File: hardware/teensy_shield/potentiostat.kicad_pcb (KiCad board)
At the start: 2 copper layers, 144.8 x 88.9 mm, 99 parts, among them K1 CONN_3, P1 CONN_2, P10 CONN_2, P11 CONN_2, P12 CONN_2, P13 CONN_5X2, P14 CONN_5X2, P15 CONN_2X2, P16 CONN_2X2, P17 CONN_2, P18 CONN_2, P19 CONN_2, P2 CONN_2, P20 CONN_2, P21 CONN_2, P3 CONN_2, P4 CONN_2, P5 CONN_2, P6 CONN_2, P7 CONN_2, P8 CONN_2, P9 CONN_2, U1 ZXRE060, U10 OPA227, U11 OP07, U12 LT1995, U13 ADG44X, U2 TEENSY3.1, U3 MAX6176AASA+, U4 LT1995, U5 AD8250, U6 MEA1D05XXSC, U7 OPA129, U8 OPA129, U9 ADG44X

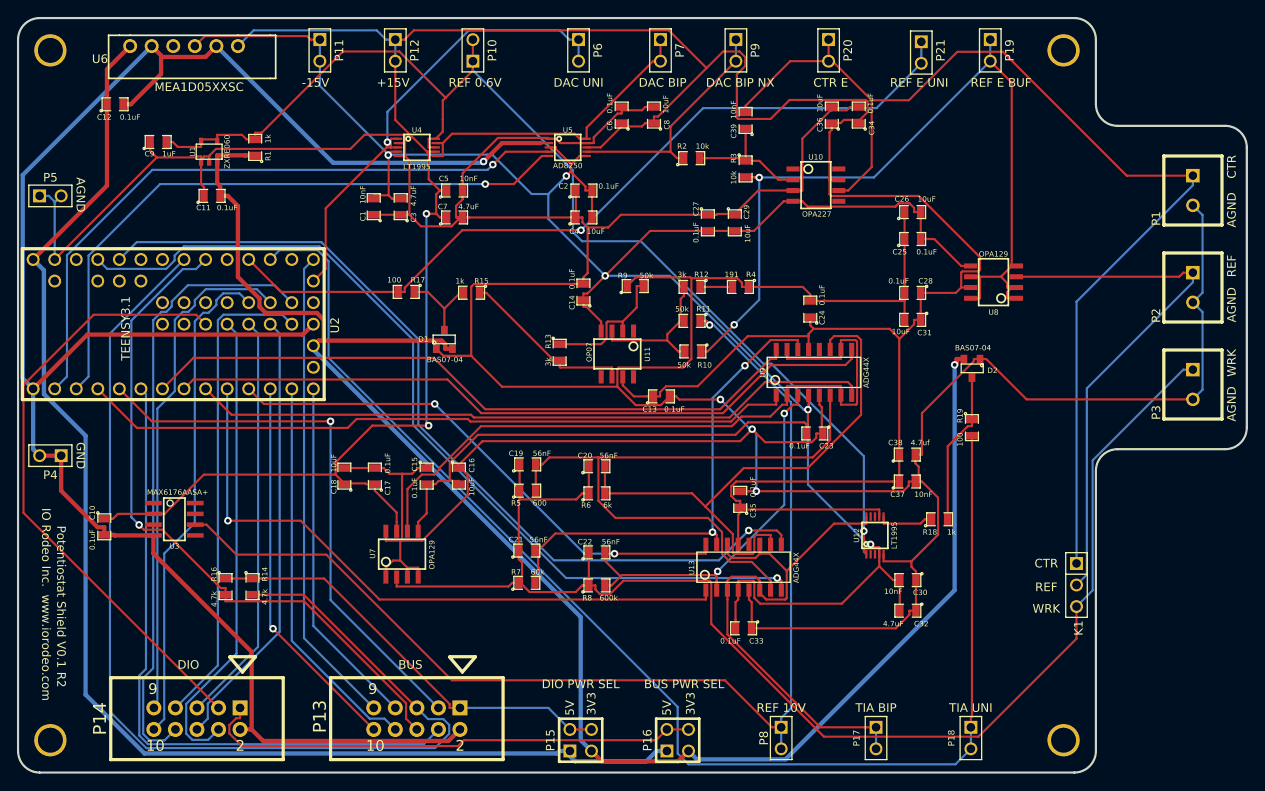
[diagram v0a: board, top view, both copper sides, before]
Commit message: Modified teensy shield BOM, layout, and gerbers per pcb manufacturers suggestions.
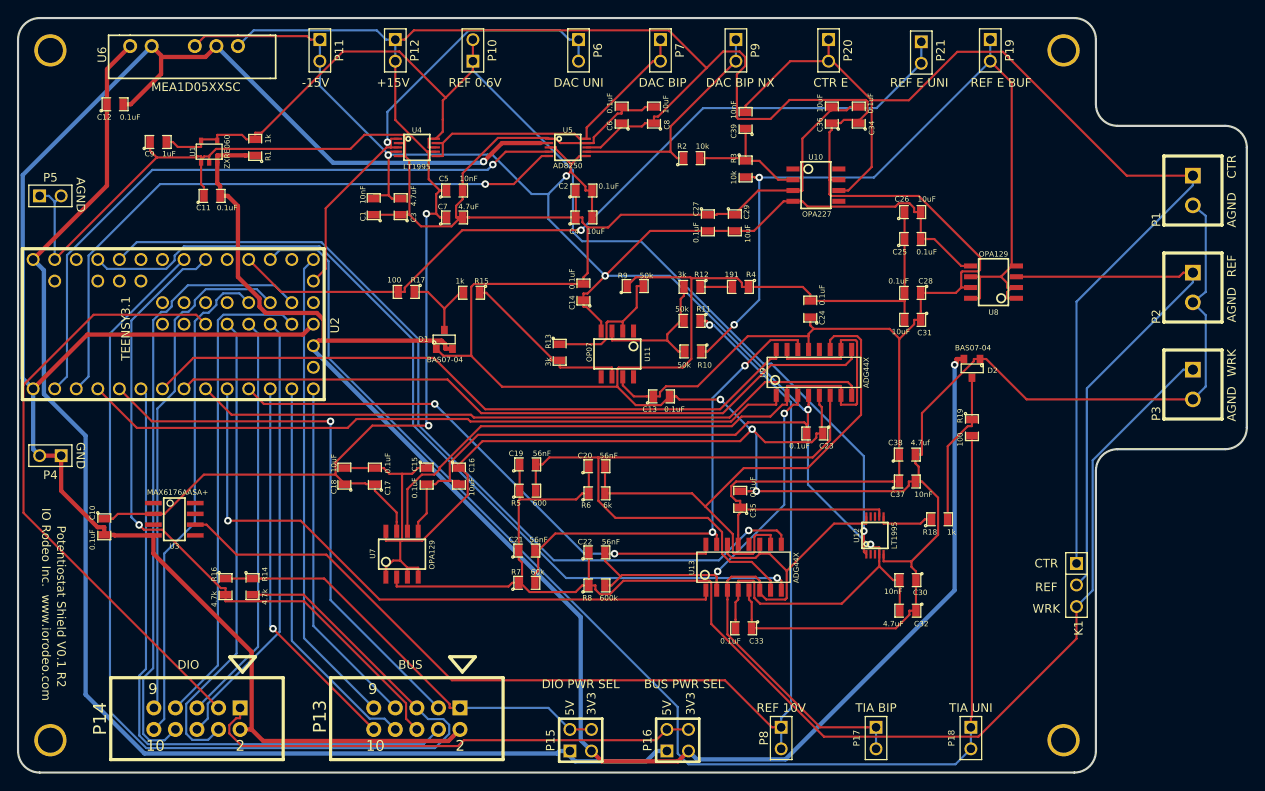
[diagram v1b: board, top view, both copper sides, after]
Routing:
- net /AGND: track 563.5 -> 564.3 mm
